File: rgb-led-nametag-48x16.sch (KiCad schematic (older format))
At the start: 64 parts, among them J1 USB_C_Receptacle_USB2.0, Q17 CJ3139K, Q18 CJ3139K, Q19 2SK3541, Q20 AO3401A, Q21 FS8205, SW1 SW_Push, SW2 SW_Push, U25 STM32F722RETx, U26 SRV05-4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

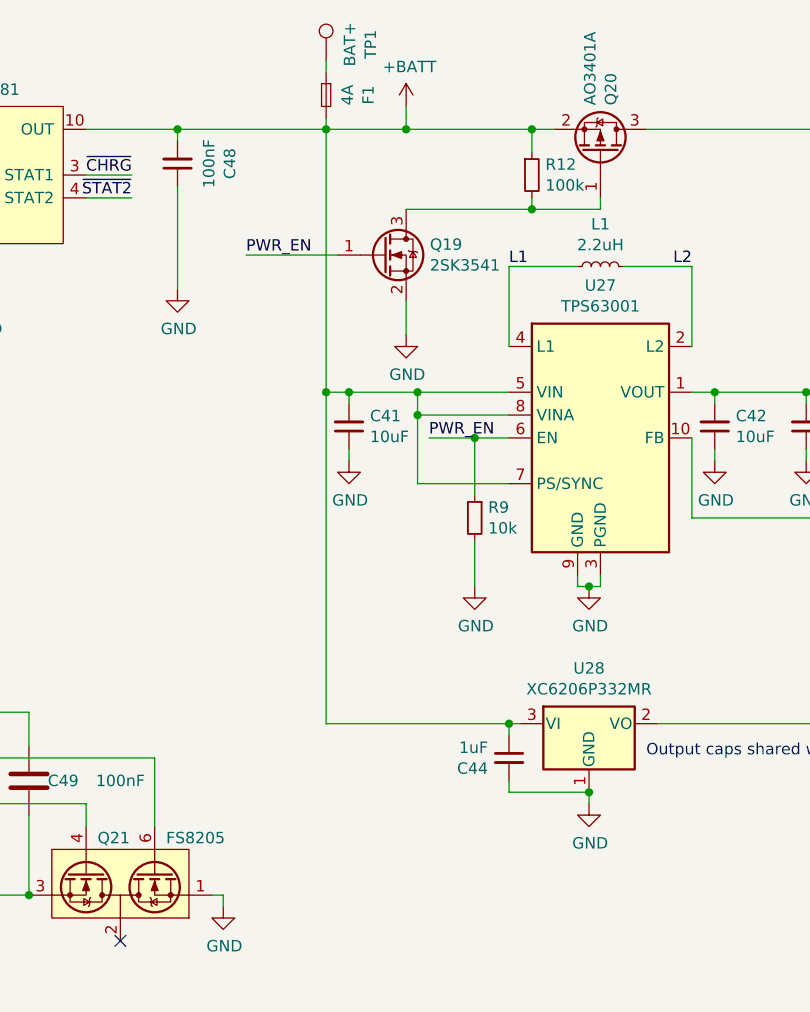
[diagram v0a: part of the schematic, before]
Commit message: Use better ESP32 Pico D4 footprint
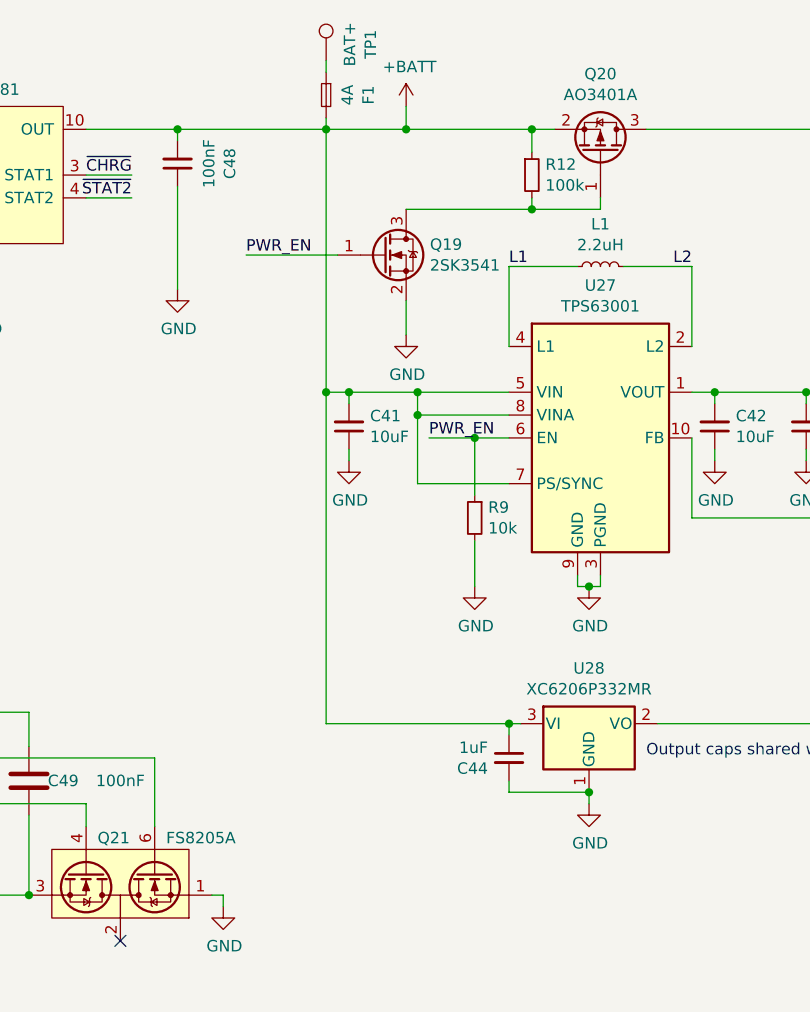
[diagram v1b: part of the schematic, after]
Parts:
- Q20: LCSC (none) -> C15127
- Q21: value FS8205 -> FS8205A; LCSC C32254 -> C2830320
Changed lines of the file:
@@
 U 1 1 62736410
 P 16050 950
-F 0 "Q20" H 16255 996 50  0000 L CNN
-F 1 "AO3401A" H 16255 905 50  0000 L CNN
+F 0 "Q20" V 16392 950 50  0000 C CNN
+F 1 "AO3401A" V 16301 950 50  0000 C CNN
 F 2 "Package_TO_SOT_SMD:SOT-23" H 16250 875 50  0001 L CIN
 F 3 "http://www.aosmd.com/pdfs/datasheet/AO3401A.pdf" H 16050 950 50  0001 L CNN
+F 4 "C15127" H 16050 950 50  0001 C CNN "LCSC"
 	1    16050 950
 	0    1    -1   0
@@
 P 13950 4200
 F 0 "Q21" H 14050 3950 50  0000 R CNN
-F 1 "FS8205" H 13750 3950 50  0000 R CNN
+F 1 "FS8205A" H 13750 3950 50  0000 R CNN
 F 2 "Package_TO_SOT_SMD:SOT-23-6" H 13950 4700 50  0001 C CNN
 F 3 "https://datasheet.lcsc.com/szlcsc/Fortune-Semicon-FS8205_C32254.pdf" H 13950 4700 50  0001 C CNN
-F 4 "C32254" H 13900 4200 50  0001 C CNN "LCSC"
+F 4 "C2830320" H 13900 4200 50  0001 C CNN "LCSC"
 	1    13950 4200
 	-1   0    0    1

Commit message: Add additional VBUS bulk capacitance
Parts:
- added C51, C52: 10uF, Capacitor_SMD:C_0402_1005Metric, symbol Device:C_Small
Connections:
- net GND: now also C51.2, C52.2
- net VBUS: now also C51.1, C52.1
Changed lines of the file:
@@
 S 2050 2800 650  900
 U 61C25DCC
-F0 "Low side 1" 50
+F0 "High side 1" 50
 F1 "high-side-driver.sch" 50
 F2 "~OE" I L 2050 3300 50
@@
 S 2050 4000 650  900
 U 61C56D3D
-F0 "sheet61C56D2D" 50
+F0 "High side 2" 50
 F1 "high-side-driver.sch" 50
 F2 "~OE" I L 2050 4500 50
@@
 Wire Wire Line
 	7400 2250 7850 2250
+Text Label 7850 2250 2    50   ~ 0
+~CHRG
+$Comp
+L Device:C_Small C?
+U 1 1 63E4DA71
+P 2400 2350
+AR Path="/620161BA/63E4DA71" Ref="C?"  Part="1"
+AR Path="/63E4DA71" Ref="C51"  Part="1"
+F 0 "C51" H 2308 2304 50  0000 R CNN
+F 1 "10uF" H 2308 2395 50  0000 R CNN
+F 2 "Capacitor_SMD:C_0402_1005Metric" H 2400 2350 50  0001 C CNN
+F 3 "~" H 2400 2350 50  0001 C CNN
+F 4 "C15525" H 2400 2350 50  0001 C CNN "LCSC"
+	1    2400 2350
+	1    0    0    -1
+$EndComp
+$Comp
+L power:GND #PWR0219
+U 1 1 63E6D392
+P 2400 2450
+F 0 "#PWR0219" H 2400 2200 50  0001 C CNN
+F 1 "GND" H 2405 2277 50  0000 C CNN
+F 2 "" H 2400 2450 50  0001 C CNN
+F 3 "" H 2400 2450 50  0001 C CNN
+	1    2400 2450
+	1    0    0    -1
+$EndComp
+$Comp
+L power:VBUS #PWR0220
+U 1 1 63E6EE0D
+P 2400 2250
+F 0 "#PWR0220" H 2400 2100 50  0001 C CNN
+F 1 "VBUS" H 2415 2423 50  0000 C CNN
+F 2 "" H 2400 2250 50  0001 C CNN
+F 3 "" H 2400 2250 50  0001 C CNN
+	1    2400 2250
+	1    0    0    -1
+$EndComp
+$Comp
+L Device:C_Small C?
+U 1 1 63E6FF8A
+P 2400 5350
+AR Path="/620161BA/63E6FF8A" Ref="C?"  Part="1"
+AR Path="/63E6FF8A" Ref="C52"  Part="1"
+F 0 "C52" H 2308 5304 50  0000 R CNN
+F 1 "10uF" H 2308 5395 50  0000 R CNN
+F 2 "Capacitor_SMD:C_0402_1005Metric" H 2400 5350 50  0001 C CNN
+F 3 "~" H 2400 5350 50  0001 C CNN
+F 4 "C15525" H 2400 5350 50  0001 C CNN "LCSC"
+	1    2400 5350
+	1    0    0    -1
+$EndComp
+$Comp
+L power:GND #PWR0221
+U 1 1 63E6FF90
+P 2400 5450
+F 0 "#PWR0221" H 2400 5200 50  0001 C CNN
+F 1 "GND" H 2405 5277 50  0000 C CNN
+F 2 "" H 2400 5450 50  0001 C CNN
+F 3 "" H 2400 5450 50  0001 C CNN
+	1    2400 5450
+	1    0    0    -1
+$EndComp
+$Comp
+L power:VBUS #PWR0222
+U 1 1 63E6FF96
+P 2400 5250
+F 0 "#PWR0222" H 2400 5100 50  0001 C CNN
+F 1 "VBUS" H 2415 5423 50  0000 C CNN
+F 2 "" H 2400 5250 50  0001 C CNN
+F 3 "" H 2400 5250 50  0001 C CNN
+	1    2400 5250
+	1    0    0    -1
+$EndComp
 Wire Bus Line
 	2950 1250 2950 6650
-Text Label 7850 2250 2    50   ~ 0
-~CHRG
 $EndSCHEMATC

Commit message: Add fuel gauge
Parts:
- added C53, C54: 1uF, Capacitor_SMD:C_0402_1005Metric, symbol Device:C_Small
- added R24, R27: 10k, Resistor_SMD:R_0402_1005Metric, symbol Device:R_Small
- added R25, R26: 5.1k, Resistor_SMD:R_0402_1005Metric, symbol Device:R_Small
- added U31: BQ27421, Package_DSBGA:DSBGA-9_1.6x1.6_P0.5mm, symbol Fuel_Gauge_TI:BQ27421
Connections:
- net +3V3: now also R25.2, R26.1, R27.2
- net +BATT: now also U31.C2 (SRX); no longer F1.2
- net GND: now also C53.2, C54.1, R24.1, U31.B2 (VSS), U31.C1 (VSS)
- net ROW_LATCH: now also U25.14 (PA0); no longer U25.28 (PB10)
- net USB_SENSE: now also U25.35 (PB14); no longer U25.29 (PB11)
- net ~CHRG: now also U25.8 (PC0); no longer U25.16 (PA2)
- net ~STAT2: now also U25.16 (PA2); no longer U25.8 (PC0)
- net GPOUT: now reaches U25.9 (PC1)
- net GPOUT: now also R27.1, U31.A1 (GPOUT)
- new net: C53.1, F1.2, U31.C3 (BAT)
- new net: R24.2, U31.B1 (BIN)
- new net: C54.2, U31.B3 (VDD)
- new net GAUGE_SCL: R25.1, U25.28 (PB10), U31.A3 (SCL)
- new net GAUGE_SDA: R26.2, U25.29 (PB11), U31.A2 (SDA)
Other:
- moved on the sheet: F1, R23, TP1

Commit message: Fix 5.1k resistor package
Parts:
- R17, R25, R26, R4, R5: LCSC C23186 -> C25905
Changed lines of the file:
@@
 F 2 "Resistor_SMD:R_0402_1005Metric" H 16550 5950 50  0001 C CNN
 F 3 "~" H 16550 5950 50  0001 C CNN
-F 4 "C23186" H 16550 5950 50  0001 C CNN "LCSC"
+F 4 "C25905" H 16550 5950 50  0001 C CNN "LCSC"
 	1    16550 5950
 	0    1    -1   0
@@
 F 2 "Resistor_SMD:R_0402_1005Metric" H 16550 5850 50  0001 C CNN
 F 3 "~" H 16550 5850 50  0001 C CNN
-F 4 "C23186" H 16550 5850 50  0001 C CNN "LCSC"
+F 4 "C25905" H 16550 5850 50  0001 C CNN "LCSC"
 	1    16550 5850
 	0    -1   1    0
@@
 F 2 "Resistor_SMD:R_0402_1005Metric" H 8900 5950 50  0001 C CNN
 F 3 "~" H 8900 5950 50  0001 C CNN
-F 4 "C23186" H 8900 5950 50  0001 C CNN "LCSC"
+F 4 "C25905" H 8900 5950 50  0001 C CNN "LCSC"
 	1    8900 5950
 	0    -1   1    0
@@
 F 2 "Resistor_SMD:R_0402_1005Metric" H 8050 4600 50  0001 C CNN
 F 3 "~" H 8050 4600 50  0001 C CNN
-F 4 "C23186" H 8050 4600 50  0001 C CNN "LCSC"
+F 4 "C25905" H 8050 4600 50  0001 C CNN "LCSC"
 	1    8050 4600
 	1    0    0    1
@@
 F 2 "Resistor_SMD:R_0402_1005Metric" H 8150 4600 50  0001 C CNN
 F 3 "~" H 8150 4600 50  0001 C CNN
-F 4 "C23186" H 8150 4600 50  0001 C CNN "LCSC"
+F 4 "C25905" H 8150 4600 50  0001 C CNN "LCSC"
 	1    8150 4600
 	-1   0    0    -1

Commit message: Connect ESD diode after SWD SBU resistors
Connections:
- net SWCLK: no longer U26.1 (IO1)
- net SWDIO: no longer U26.3 (IO2)
- net SWDIO_SBU: now reaches J1.A8 (SBU1), R15.2
- net SWDIO_SBU: now also U26.3 (IO2)
- net SWCLK_SBU: now reaches J1.B8 (SBU2), R16.1
- net SWCLK_SBU: now also U26.1 (IO1)
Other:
- moved on the sheet: R15, R16, U26
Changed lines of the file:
@@
 Wire Wire Line
 	17000 5600 17000 5650
-Text Label 10050 3800 2    50   ~ 0
+Text Label 10400 3750 2    50   ~ 0
 D+
 Wire Wire Line
-	9850 3800 10050 3800
-Text Label 10050 4000 2    50   ~ 0
+	10200 3750 10400 3750
+Text Label 10400 3950 2    50   ~ 0
 D-
 Wire Wire Line
-	9850 4000 10050 4000
+	10200 3950 10400 3950
 $Comp
 L Power_Protection:SRV05-4 U26
 U 1 1 61FD5228
-P 9350 3900
-F 0 "U26" H 9150 4400 50  0000 C CNN
-F 1 "SRV05-4" H 9600 4400 50  0000 C CNN
-F 2 "Package_TO_SOT_SMD:SOT-23-6" H 10050 3450 50  0001 C CNN
-F 3 "http://www.onsemi.com/pub/Collateral/SRV05-4-D.PDF" H 9350 3900 50  0001 C CNN
-F 4 "C85364" H 9350 3900 50  0001 C CNN "LCSC"
-	1    9350 3900
+P 9700 3850
+F 0 "U26" H 9500 4350 50  0000 C CNN
+F 1 "SRV05-4" H 9950 4350 50  0000 C CNN
+F 2 "Package_TO_SOT_SMD:SOT-23-6" H 10400 3400 50  0001 C CNN
+F 3 "http://www.onsemi.com/pub/Collateral/SRV05-4-D.PDF" H 9700 3850 50  0001 C CNN
+F 4 "C85364" H 9700 3850 50  0001 C CNN "LCSC"
+	1    9700 3850
 	1    0    0    -1
 $EndComp
@@
 SWCLK
 Wire Wire Line
-	16650 6750 17100 6750
-Text Label 17100 6750 2    50   ~ 0
+	17050 6750 17500 6750
+Text Label 17500 6750 2    50   ~ 0
 SWDIO
 Wire Wire Line
-	16650 6850 17100 6850
-Text Label 17100 6850 2    50   ~ 0
+	17050 6850 17500 6850
+Text Label 17500 6850 2    50   ~ 0
 SWCLK
-Text Label 8600 3800 0    50   ~ 0
-SWCLK
-Wire Wire Line
-	8600 3800 8850 3800
+Text Label 8800 3750 0    50   ~ 0
+SWCLK_SBU
 $Comp
 L Device:R_Small R15
 U 1 1 62A6EAFE
-P 16550 6750
-F 0 "R15" V 16746 6750 50  0000 C CNN
-F 1 "470R" V 16655 6750 50  0000 C CNN
-F 2 "Resistor_SMD:R_0402_1005Metric" H 16550 6750 50  0001 C CNN
-F 3 "~" H 16550 6750 50  0001 C CNN
-F 4 "C25117" H 16550 6750 50  0001 C CNN "LCSC"
-	1    16550 6750
+P 16950 6750
+F 0 "R15" V 17146 6750 50  0000 C CNN
+F 1 "470R" V 17055 6750 50  0000 C CNN
+F 2 "Resistor_SMD:R_0402_1005Metric" H 16950 6750 50  0001 C CNN
+F 3 "~" H 16950 6750 50  0001 C CNN
+F 4 "C25117" H 16950 6750 50  0001 C CNN "LCSC"
+	1    16950 6750
 	0    1    -1   0
 $EndComp
@@
 L Device:R_Small R16
 U 1 1 62A82547
-P 16550 6850
-F 0 "R16" V 16746 6850 50  0000 C CNN
-F 1 "470R" V 16655 6850 50  0000 C CNN
-F 2 "Resistor_SMD:R_0402_1005Metric" H 16550 6850 50  0001 C CNN
-F 3 "~" H 16550 6850 50  0001 C CNN
-F 4 "C25117" H 16550 6850 50  0001 C CNN "LCSC"
-	1    16550 6850
+P 16950 6850
+F 0 "R16" V 17146 6850 50  0000 C CNN
+F 1 "470R" V 17055 6850 50  0000 C CNN
+F 2 "Resistor_SMD:R_0402_1005Metric" H 16950 6850 50  0001 C CNN
+F 3 "~" H 16950 6850 50  0001 C CNN
+F 4 "C25117" H 16950 6850 50  0001 C CNN "LCSC"
+	1    16950 6850
 	0    -1   1    0
 $EndComp
-Wire Wire Line
-	16450 6750 16400 6750
-Wire Wire Line
-	16400 6850 16450 6850
-Wire Wire Line
-	8600 4000 8850 4000
-Text Label 8600 4000 0    50   ~ 0
-SWDIO
+Text Label 8800 3950 0    50   ~ 0
+SWDIO_SBU
 $Comp
 L Device:C_Small C?
@@
 L power:+5V #PWR0199
 U 1 1 62C054E2
-P 9350 3350
-F 0 "#PWR0199" H 9350 3200 50  0001 C CNN
-F 1 "+5V" H 9365 3523 50  0000 C CNN
-F 2 "" H 9350 3350 50  0001 C CNN
-F 3 "" H 9350 3350 50  0001 C CNN
-	1    9350 3350
-	1    0    0    -1
-$EndComp
-Wire Wire Line
-	9350 3400 9350 3350
+P 9700 3300
+F 0 "#PWR0199" H 9700 3150 50  0001 C CNN
+F 1 "+5V" H 9715 3473 50  0000 C CNN
+F 2 "" H 9700 3300 50  0001 C CNN
+F 3 "" H 9700 3300 50  0001 C CNN
+	1    9700 3300
+	1    0    0    -1
+$EndComp
+Wire Wire Line
+	9700 3350 9700 3300
 $Comp
 L power:GND #PWR0200
 U 1 1 62C1B8E9
-P 9350 4450
-F 0 "#PWR0200" H 9350 4200 50  0001 C CNN
-F 1 "GND" H 9355 4277 50  0000 C CNN
-F 2 "" H 9350 4450 50  0001 C CNN
-F 3 "" H 9350 4450 50  0001 C CNN
-	1    9350 4450
+P 9700 4400
+F 0 "#PWR0200" H 9700 4150 50  0001 C CNN
+F 1 "GND" H 9705 4227 50  0000 C CNN
+F 2 "" H 9700 4400 50  0001 C CNN
+F 3 "" H 9700 4400 50  0001 C CNN
+	1    9700 4400
 	1    0    0    -1
 $EndComp
@@
 	7400 2050 7850 2050
 Wire Wire Line
-	9350 4450 9350 4400
+	9700 4400 9700 4350
 Text Label 7850 5250 2    50   ~ 0
 SPI2_MOSI
@@
 Wire Wire Line
 	5550 3650 5550 3700
+Text Label 16850 6750 2    50   ~ 0
+SWDIO_SBU
+Wire Wire Line
+	16400 6750 16850 6750
+Wire Wire Line
+	16400 6850 16850 6850
+Text Label 16850 6850 2    50   ~ 0
+SWCLK_SBU
+Wire Wire Line
+	8800 3750 9200 3750
+Wire Wire Line
+	8800 3950 9200 3950
 Wire Bus Line
 	2950 1250 2950 6650

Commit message: Fix row/column misnomer
The row/column terms were swapped. The high side drivers control columns
while the low side drivers switch the rows.
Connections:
- net COL_LATCH: now also U25.14 (PA0); no longer U25.37 (PC6)
- net ROW_LATCH: now also U25.37 (PC6); no longer U25.14 (PA0)
- net COL_~OE renamed ROW_~OE
- net COL_~RST: no longer names the net of U25.39 (PC8)
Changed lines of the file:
@@
 QSPI_CLK
 Text Label 4550 1550 2    50   ~ 0
-COL_~OE
+ROW_~OE
 Text Label 7850 2550 2    50   ~ 0
 SPI1_CLK
@@
 Connection ~ 1750 3100
 Text Label 1150 3100 0    50   ~ 0
+COL_LATCH
+Text Label 4550 1350 2    50   ~ 0
 ROW_LATCH
-Text Label 4550 1350 2    50   ~ 0
-COL_LATCH
 Wire Wire Line
 	4100 1350 4550 1350
@@
 QSPI_CLK
 Text Label 4550 3500 2    50   ~ 0
-COL_~OE
+ROW_~OE
 Text Label 4550 3300 2    50   ~ 0
-COL_LATCH
+ROW_LATCH
 Wire Wire Line
 	4100 3300 4550 3300
@@
 QSPI_CLK
 Text Label 4550 5450 2    50   ~ 0
-COL_~OE
+ROW_~OE
 Text Label 4550 5250 2    50   ~ 0
-COL_LATCH
+ROW_LATCH
 Wire Wire Line
 	4100 5250 4550 5250
@@
 	4100 5450 4550 5450
 Text Label 5650 4350 0    50   ~ 0
-COL_LATCH
+ROW_LATCH
 Wire Wire Line
 	6100 4350 5650 4350
 Text Label 5650 4450 0    50   ~ 0
-COL_~OE
+ROW_~OE
 Wire Wire Line
 	6100 4450 5650 4450
@@
 Wire Wire Line
 	5650 4750 6100 4750
-Wire Wire Line
-	6100 4550 5650 4550
-Text Label 5650 4550 0    50   ~ 0
-COL_~RST
 NoConn ~ 7400 3550
 Text Notes 6900 3550 0    50   ~ 0
@@
 SPI2_CLK
 Text Label 7850 2050 2    50   ~ 0
-ROW_LATCH
+COL_LATCH
 Wire Wire Line
 	7400 3750 7850 3750

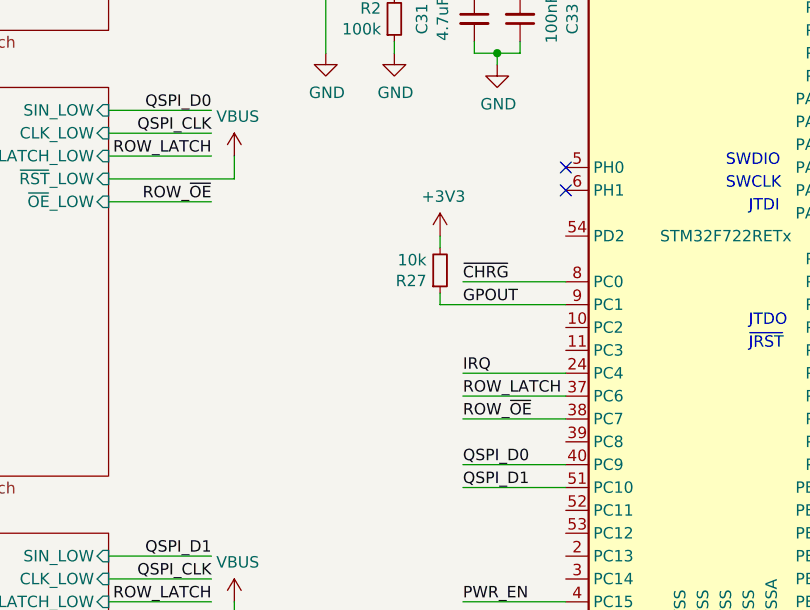
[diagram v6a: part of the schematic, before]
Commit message: Add 16MHz crystal
Turns out the STM32F7 DFU bootloader uses the HSE for USB clocking and
thus requires a crystal. No fallback to HSI is implemented. *sigh*
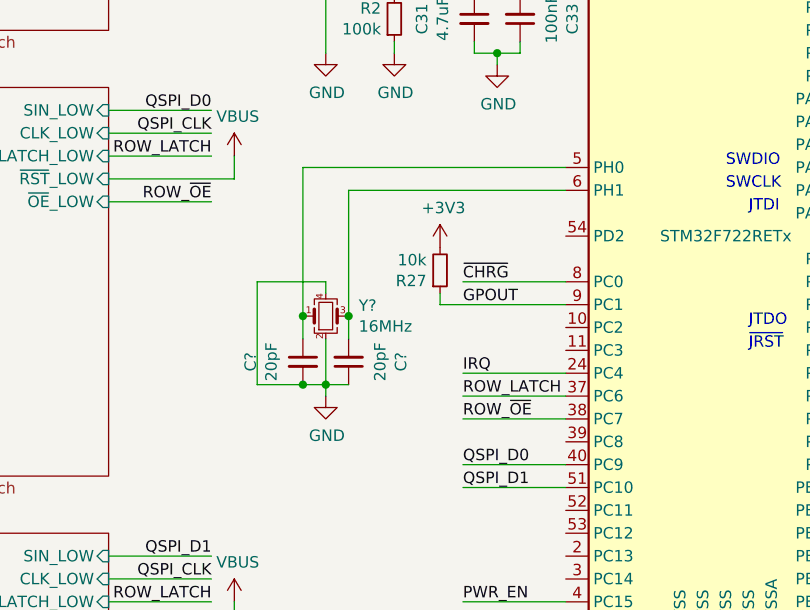
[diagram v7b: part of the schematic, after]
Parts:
- added C? (x2): 20pF, Capacitor_SMD:C_0402_1005Metric, symbol Device:C_Small
- added Y?: 16MHz, Crystal:Crystal_SMD_3225-4Pin_3.2x2.5mm, symbol Device:Crystal_GND24_Small
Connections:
- net GND: now also C?.1, C?.2, Y?.2, Y?.4
- net at U25.5 (PH0): now also C?.1, Y?.1
- net at U25.6 (PH1): now also C?.2, Y?.3
- no-connect marks 8 -> 6
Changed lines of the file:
@@
 Text Label 7850 3050 2    50   ~ 0
 RX
-NoConn ~ 6100 3350
-NoConn ~ 6100 3450
 $Comp
 L Device:R_Small R5
@@
 L power:+3V3 #PWR0228
 U 1 1 649479C6
-P 5550 3650
-F 0 "#PWR0228" H 5550 3500 50  0001 C CNN
-F 1 "+3V3" H 5565 3823 50  0000 C CNN
-F 2 "" H 5550 3650 50  0001 C CNN
-F 3 "" H 5550 3650 50  0001 C CNN
-	1    5550 3650
-	1    0    0    -1
-$EndComp
-Wire Wire Line
-	5550 3650 5550 3700
+P 5550 3700
+F 0 "#PWR0228" H 5550 3550 50  0001 C CNN
+F 1 "+3V3" H 5565 3873 50  0000 C CNN
+F 2 "" H 5550 3700 50  0001 C CNN
+F 3 "" H 5550 3700 50  0001 C CNN
+	1    5550 3700
+	1    0    0    -1
+$EndComp
 Text Label 16850 6750 2    50   ~ 0
 SWDIO_SBU
@@
 Wire Wire Line
 	8800 3950 9200 3950
+$Comp
+L Device:C_Small C?
+U 1 1 61D19B39
+P 5150 4200
+AR Path="/61A41C1D/61A5C767/61D19B39" Ref="C?"  Part="1"
+AR Path="/61A41C1D/61A68DB0/61D19B39" Ref="C?"  Part="1"
+AR Path="/61A41C1D/61A6C361/61D19B39" Ref="C?"  Part="1"
+AR Path="/61A41C1D/61A75B5D/61D19B39" Ref="C?"  Part="1"
+AR Path="/61A41C1D/61A75B6D/61D19B39" Ref="C?"  Part="1"
+AR Path="/61A41C1D/61A75B93/61D19B39" Ref="C?"  Part="1"
+AR Path="/61C4C20D/61A5C767/61D19B39" Ref="C?"  Part="1"
+AR Path="/61C4C20D/61A68DB0/61D19B39" Ref="C?"  Part="1"
+AR Path="/61C4C20D/61A6C361/61D19B39" Ref="C?"  Part="1"
+AR Path="/61C4C20D/61A75B5D/61D19B39" Ref="C?"  Part="1"
+AR Path="/61C4C20D/61A75B6D/61D19B39" Ref="C?"  Part="1"
+AR Path="/61C4C20D/61A75B93/61D19B39" Ref="C?"  Part="1"
+AR Path="/61C4C905/61A5C767/61D19B39" Ref="C?"  Part="1"
+AR Path="/61C4C905/61A68DB0/61D19B39" Ref="C?"  Part="1"
+AR Path="/61C4C905/61A6C361/61D19B39" Ref="C?"  Part="1"
+AR Path="/61C4C905/61A75B5D/61D19B39" Ref="C?"  Part="1"
+AR Path="/61C4C905/61A75B6D/61D19B39" Ref="C?"  Part="1"
+AR Path="/61C4C905/61A75B93/61D19B39" Ref="C?"  Part="1"
+AR Path="/61D19B39" Ref="C?"  Part="1"
+F 0 "C?" V 4921 4200 50  0000 C CNN
+F 1 "20pF" V 5012 4200 50  0000 C CNN
+F 2 "Capacitor_SMD:C_0402_1005Metric" H 5150 4200 50  0001 C CNN
+F 3 "~" H 5150 4200 50  0001 C CNN
+F 4 "C1554" V 5150 4200 50  0001 C CNN "LCSC"
+	1    5150 4200
+	-1   0    0    1
+$EndComp
+$Comp
+L Device:Crystal_GND24_Small Y?
+U 1 1 61D3E707
+P 5050 4000
+F 0 "Y?" H 5194 4046 50  0000 L CNN
+F 1 "16MHz" H 5194 3955 50  0000 L CNN
+F 2 "Crystal:Crystal_SMD_3225-4Pin_3.2x2.5mm" H 5050 4000 50  0001 C CNN
+F 3 "https://datasheet.lcsc.com/szlcsc/Yangxing-Tech-X322516MLB4SI_C13738.pdf" H 5050 4000 50  0001 C CNN
+F 4 "C13738" H 5050 4000 50  0001 C CNN "LCSC"
+	1    5050 4000
+	1    0    0    -1
+$EndComp
+$Comp
+L Device:C_Small C?
+U 1 1 61DAAE1C
+P 4950 4200
+AR Path="/61A41C1D/61A5C767/61DAAE1C" Ref="C?"  Part="1"
+AR Path="/61A41C1D/61A68DB0/61DAAE1C" Ref="C?"  Part="1"
+AR Path="/61A41C1D/61A6C361/61DAAE1C" Ref="C?"  Part="1"
+AR Path="/61A41C1D/61A75B5D/61DAAE1C" Ref="C?"  Part="1"
+AR Path="/61A41C1D/61A75B6D/61DAAE1C" Ref="C?"  Part="1"
+AR Path="/61A41C1D/61A75B93/61DAAE1C" Ref="C?"  Part="1"
+AR Path="/61C4C20D/61A5C767/61DAAE1C" Ref="C?"  Part="1"
+AR Path="/61C4C20D/61A68DB0/61DAAE1C" Ref="C?"  Part="1"
+AR Path="/61C4C20D/61A6C361/61DAAE1C" Ref="C?"  Part="1"
+AR Path="/61C4C20D/61A75B5D/61DAAE1C" Ref="C?"  Part="1"
+AR Path="/61C4C20D/61A75B6D/61DAAE1C" Ref="C?"  Part="1"
+AR Path="/61C4C20D/61A75B93/61DAAE1C" Ref="C?"  Part="1"
+AR Path="/61C4C905/61A5C767/61DAAE1C" Ref="C?"  Part="1"
+AR Path="/61C4C905/61A68DB0/61DAAE1C" Ref="C?"  Part="1"
+AR Path="/61C4C905/61A6C361/61DAAE1C" Ref="C?"  Part="1"
+AR Path="/61C4C905/61A75B5D/61DAAE1C" Ref="C?"  Part="1"
+AR Path="/61C4C905/61A75B6D/61DAAE1C" Ref="C?"  Part="1"
+AR Path="/61C4C905/61A75B93/61DAAE1C" Ref="C?"  Part="1"
+AR Path="/61DAAE1C" Ref="C?"  Part="1"
+F 0 "C?" V 4721 4200 50  0000 C CNN
+F 1 "20pF" V 4812 4200 50  0000 C CNN
+F 2 "Capacitor_SMD:C_0402_1005Metric" H 4950 4200 50  0001 C CNN
+F 3 "~" H 4950 4200 50  0001 C CNN
+F 4 "C1554" V 4950 4200 50  0001 C CNN "LCSC"
+	1    4950 4200
+	1    0    0    -1
+$EndComp
+$Comp
+L power:GND #PWR?
+U 1 1 61DCED95
+P 5050 4350
+F 0 "#PWR?" H 5050 4100 50  0001 C CNN
+F 1 "GND" H 5055 4177 50  0000 C CNN
+F 2 "" H 5050 4350 50  0001 C CNN
+F 3 "" H 5050 4350 50  0001 C CNN
+	1    5050 4350
+	1    0    0    -1
+$EndComp
+Wire Wire Line
+	5050 4350 5050 4300
+Wire Wire Line
+	5050 4300 4950 4300
+Wire Wire Line
+	5050 4300 5150 4300
+Connection ~ 5050 4300
+Wire Wire Line
+	5050 4100 5050 4300
+Wire Wire Line
+	5150 4100 5150 4000
+Wire Wire Line
+	4950 4100 4950 4000
+Wire Wire Line
+	5050 3900 5050 3850
+Wire Wire Line
+	5050 3850 4750 3850
+Wire Wire Line
+	4750 3850 4750 4300
+Wire Wire Line
+	4750 4300 4950 4300
+Connection ~ 4950 4300
+Wire Wire Line
+	5150 4000 5150 3450
+Wire Wire Line
+	5150 3450 6100 3450
+Connection ~ 5150 4000
+Wire Wire Line
+	6100 3350 4950 3350
+Wire Wire Line
+	4950 3350 4950 4000
 Wire Bus Line
 	2950 1250 2950 6650
+Connection ~ 4950 4000
 $EndSCHEMATC
